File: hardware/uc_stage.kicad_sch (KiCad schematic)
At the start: 0 parts

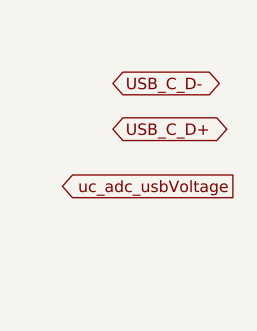
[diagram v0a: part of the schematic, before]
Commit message: More simulation and work done on SEPIC stage. MOSFET changes to USB stage and charging stage.
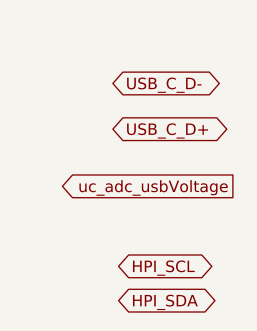
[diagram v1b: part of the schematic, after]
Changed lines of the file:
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@@
-(kicad_sch (version 20230121) (generator eeschema)
-  (paper "A4")
-  (global_label "uC_dig_STAT2" (shape output) (at 36.195 24.765 180) (fields_autoplaced)
-    (effects (font (size 1.27 1.27)) (justify right))
-    (property "Intersheetrefs" "${INTERSHEET_REFS}" (at 20.5894 24.765 0)
-      (effects (font (size 1.27 1.27)) (justify right) hide)
-    )
-  )
-  (global_label "uc_adc_usbVoltage" (shape output) (at 38.1 53.34 180) (fields_autoplaced)
-    (effects (font (size 1.27 1.27)) (justify right))
-    (property "Intersheetrefs" "${INTERSHEET_REFS}" (at 17.2936 53.34 0)
-      (effects (font (size 1.27 1.27)) (justify right) hide)
-    )
-  )
-  (global_label "uC_dig_STAT1" (shape output) (at 36.195 19.685 180) (fields_autoplaced)
-    (effects (font (size 1.27 1.27)) (justify right))
-    (property "Intersheetrefs" "${INTERSHEET_REFS}" (at 20.5894 19.685 0)
-      (effects (font (size 1.27 1.27)) (justify right) hide)
-    )
-  )
-  (global_label "USB_C_D-" (shape bidirectional) (at 24.765 41.91 0) (fields_autoplaced)
-    (effects (font (size 1.27 1.27)) (justify left))
-    (property "Intersheetrefs" "${INTERSHEET_REFS}" (at 38.6397 41.91 0)
-      (effects (font (size 1.27 1.27)) (justify left) hide)
-    )
-  )
-  (global_label "uC_dig_nPG" (shape output) (at 36.195 30.48 180) (fields_autoplaced)
-    (effects (font (size 1.27 1.27)) (justify right))
-    (property "Intersheetrefs" "${INTERSHEET_REFS}" (at 22.3432 30.48 0)
-      (effects (font (size 1.27 1.27)) (justify right) hide)
-    )
-  )
-  (global_label "USB_C_D+" (shape bidirectional) (at 24.765 46.99 0) (fields_autoplaced)
-    (effects (font (size 1.27 1.27)) (justify left))
-    (property "Intersheetrefs" "${INTERSHEET_REFS}" (at 38.6397 46.99 0)
-      (effects (font (size 1.27 1.27)) (justify left) hide)
-    )
-  )
+(kicad_sch
+	(version 20231120)
+	(generator "eeschema")
+	(generator_version "8.0")
+	(paper "A4")
+	(global_label "HPI_SCL"
+		(shape bidirectional)
+		(at 25.4 62.23 0)
+		(fields_autoplaced yes)
+		(effects
+			(font
+				(size 1.27 1.27)
+			)
+			(justify left)
+		)
+		(property "Intersheetrefs" "${INTERSHEET_REFS}"
+			(at 37.177 62.23 0)
+			(effects
+				(font
+					(size 1.27 1.27)
+				)
+				(justify left)
+				(hide yes)
+			)
+		)
+	)
+	(global_label "uC_dig_STAT2"
+		(shape output)
+		(at 36.195 24.765 180)
+		(fields_autoplaced yes)
+		(effects
+			(font
+				(size 1.27 1.27)
+			)
+			(justify right)
+		)
+		(property "Intersheetrefs" "${INTERSHEET_REFS}"
+			(at 20.5894 24.765 0)
+			(effects
+				(font
+					(size 1.27 1.27)
+				)
+				(justify right)
+				(hide yes)
+			)
+		)
+	)
+	(global_label "uc_adc_usbVoltage"
+		(shape output)
+		(at 38.1 53.34 180)
+		(fields_autoplaced yes)
+		(effects
+			(font
+				(size 1.27 1.27)
+			)
+			(justify right)
+		)
+		(property "Intersheetrefs" "${INTERSHEET_REFS}"
+			(at 17.2936 53.34 0)
+			(effects
+				(font
+					(size 1.27 1.27)
+				)
+				(justify right)
+				(hide yes)
+			)
+		)
+	)
+	(global_label "uC_dig_STAT1"
+		(shape output)
+		(at 36.195 19.685 180)
+		(fields_autoplaced yes)
+		(effects
+			(font
+				(size 1.27 1.27)
+			)
+			(justify right)
+		)
+		(property "Intersheetrefs" "${INTERSHEET_REFS}"
+			(at 20.5894 19.685 0)
+			(effects
+				(font
+					(size 1.27 1.27)
+				)
+				(justify right)
+				(hide yes)
+			)
+		)
+	)
+	(global_label "USB_C_D-"
+		(shape bidirectional)
+		(at 24.765 41.91 0)
+		(fields_autoplaced yes)
+		(effects
+			(font
+				(size 1.27 1.27)
+			)
+			(justify left)
+		)
+		(property "Intersheetrefs" "${INTERSHEET_REFS}"
+			(at 38.6397 41.91 0)
+			(effects
+				(font
+					(size 1.27 1.27)
+				)
+				(justify left)
+				(hide yes)
+			)
+		)
+	)
+	(global_label "uC_dig_nPG"
+		(shape output)
+		(at 36.195 30.48 180)
+		(fields_autoplaced yes)
+		(effects
+			(font
+				(size 1.27 1.27)
+			)
+			(justify right)
+		)
+		(property "Intersheetrefs" "${INTERSHEET_REFS}"
+			(at 22.3432 30.48 0)
+			(effects
+				(font
+					(size 1.27 1.27)
+				)
+				(justify right)
+				(hide yes)
+			)
+		)
+	)
+	(global_label "HPI_SDA"
+		(shape bidirectional)
+		(at 25.4 66.04 0)
+		(fields_autoplaced yes)
+		(effects
+			(font
+				(size 1.27 1.27)
+			)
+			(justify left)
+		)
+		(property "Intersheetrefs" "${INTERSHEET_REFS}"
+			(at 37.1581 66.04 0)
+			(effects
+				(font
+					(size 1.27 1.27)
+				)
+				(justify left)
+				(hide yes)
+			)
+		)
+	)
+	(global_label "USB_C_D+"
+		(shape bidirectional)
+		(at 24.765 46.99 0)
+		(fields_autoplaced yes)
+		(effects
+			(font
+				(size 1.27 1.27)
+			)
+			(justify left)
+		)
+		(property "Intersheetrefs" "${INTERSHEET_REFS}"
+			(at 38.6397 46.99 0)
+			(effects
+				(font
+					(size 1.27 1.27)
+				)
+				(justify left)
+				(hide yes)
+			)
+		)
+	)
 )
